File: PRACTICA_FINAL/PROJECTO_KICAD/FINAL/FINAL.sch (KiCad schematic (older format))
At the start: 0 parts

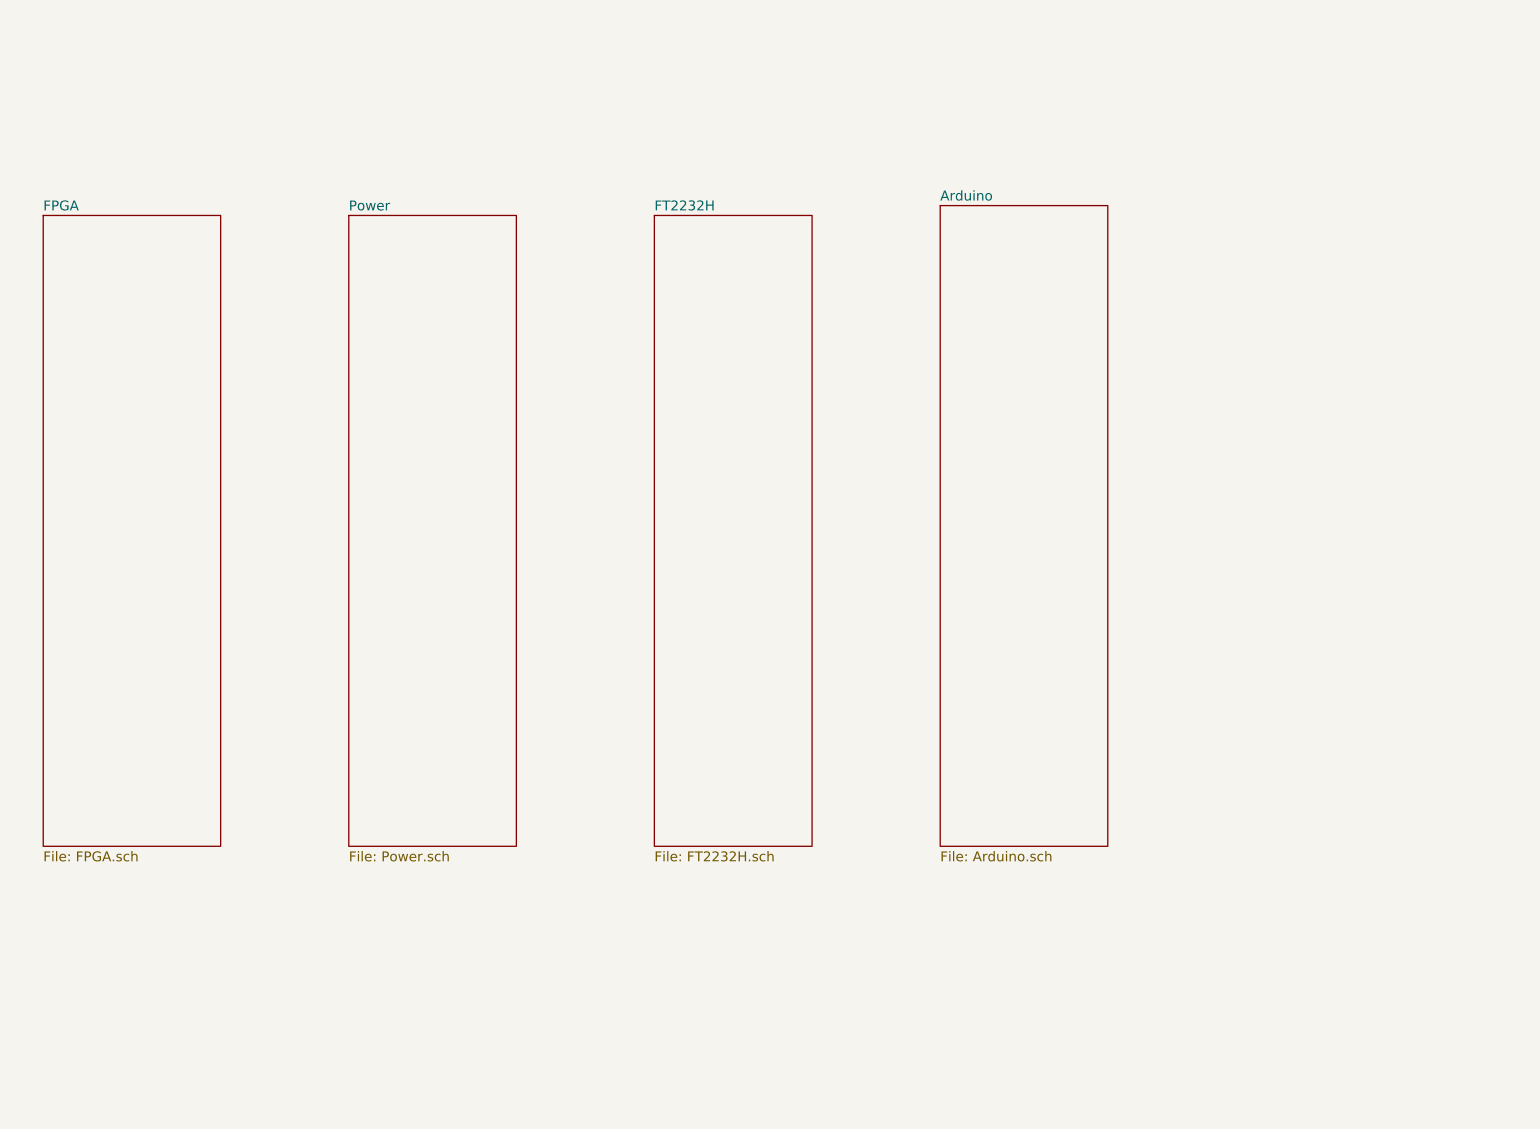
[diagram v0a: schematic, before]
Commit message: Terminada la hoja del FTDI y POWER y Arduino.bak FPGA terminado Power y Pheripheral. Lo principal de la cuestion del bnloque FPGA estan puestos los componentyes. Queda revisar globales y pasarlas a locales despues de eso. Un proyecto con muchas cosas globales se hace muy dificil de seguir.
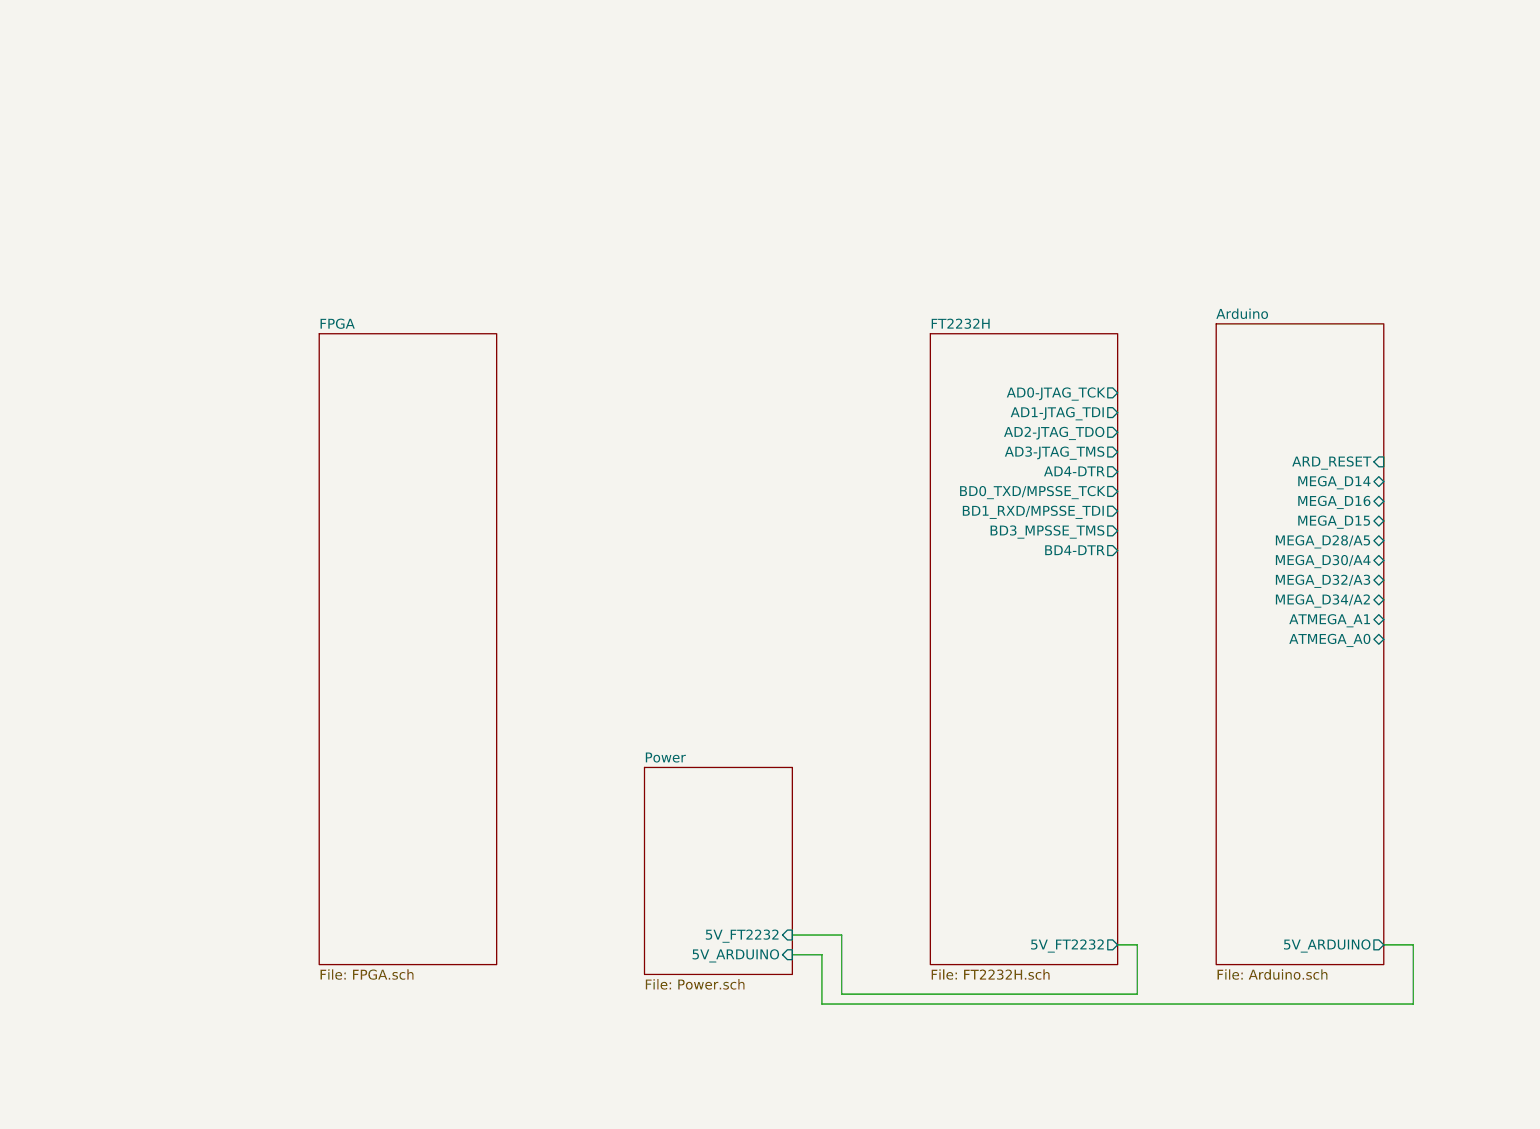
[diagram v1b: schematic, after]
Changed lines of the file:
@@
 EESchema Schematic File Version 4
+LIBS:FINAL-cache
 EELAYER 26 0
 EELAYER END
 $Descr A4 11693 8268
 encoding utf-8
-Sheet 1 5
+Sheet 1 8
 Title "Papillio Due - Clone"
 Date "2018-10-06"
@@
 $EndDescr
 $Sheet
-S 1800 1550 900  3200
+S 3200 2150 900  3200
 U 5BB93344
 F0 "FPGA" 50
@@
 $EndSheet
 $Sheet
-S 3350 1550 850  3200
+S 4850 4350 750  1050
 U 5BB93347
 F0 "Power" 50
 F1 "Power.sch" 50
+F2 "5V_ARDUINO" I R 5600 5300 50
+F3 "5V_FT2232" I R 5600 5200 50
 $EndSheet
 $Sheet
-S 4900 1550 800  3200
+S 6300 2150 950  3200
 U 5BB9334A
 F0 "FT2232H" 50
 F1 "FT2232H.sch" 50
+F2 "AD0-JTAG_TCK" O R 7250 2450 50
+F3 "AD1-JTAG_TDI" O R 7250 2550 50
+F4 "AD2-JTAG_TDO" O R 7250 2650 50
+F5 "AD3-JTAG_TMS" O R 7250 2750 50
+F6 "AD4-DTR" O R 7250 2850 50
+F7 "BD0_TXD/MPSSE_TCK" O R 7250 2950 50
+F8 "BD1_RXD/MPSSE_TDI" O R 7250 3050 50
+F9 "BD3_MPSSE_TMS" O R 7250 3150 50
+F10 "BD4-DTR" O R 7250 3250 50
+F11 "5V_FT2232" O R 7250 5250 50
 $EndSheet
 $Sheet
-S 6350 1500 850  3250
+S 7750 2100 850  3250
 U 5BB9334D
 F0 "Arduino" 50
 F1 "Arduino.sch" 50
+F2 "ARD_RESET" I R 8600 2800 50
+F3 "MEGA_D14" B R 8600 2900 50
+F4 "MEGA_D16" B R 8600 3000 50
+F5 "MEGA_D15" B R 8600 3100 50
+F6 "MEGA_D28/A5" B R 8600 3200 50
+F7 "MEGA_D30/A4" B R 8600 3300 50
+F8 "MEGA_D32/A3" B R 8600 3400 50
+F9 "MEGA_D34/A2" B R 8600 3500 50
+F10 "ATMEGA_A1" B R 8600 3600 50
+F11 "ATMEGA_A0" B R 8600 3700 50
+F12 "5V_ARDUINO" O R 8600 5250 50
 $EndSheet
+Wire Wire Line
+	5850 5500 7350 5500
+Wire Wire Line
+	7350 5500 7350 5250
+Wire Wire Line
+	7350 5250 7250 5250
+Wire Wire Line
+	5600 5300 5750 5300
+Wire Wire Line
+	5750 5300 5750 5550
+Wire Wire Line
+	5750 5550 8750 5550
+Wire Wire Line
+	8750 5550 8750 5250
+Wire Wire Line
+	8750 5250 8600 5250
+Wire Wire Line
+	5850 5200 5850 5500
+Wire Wire Line
+	5850 5200 5600 5200
 $EndSCHEMATC

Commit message: Actualizado el esquematico se enumera igual que el pdf. Se asignan todas las huellas lo unico que falta es la huella de un Arduino superpuesto Se corre DRC de esquematico y tambien se pasa a .NET y se levanta en el Kicad PCB sin errores
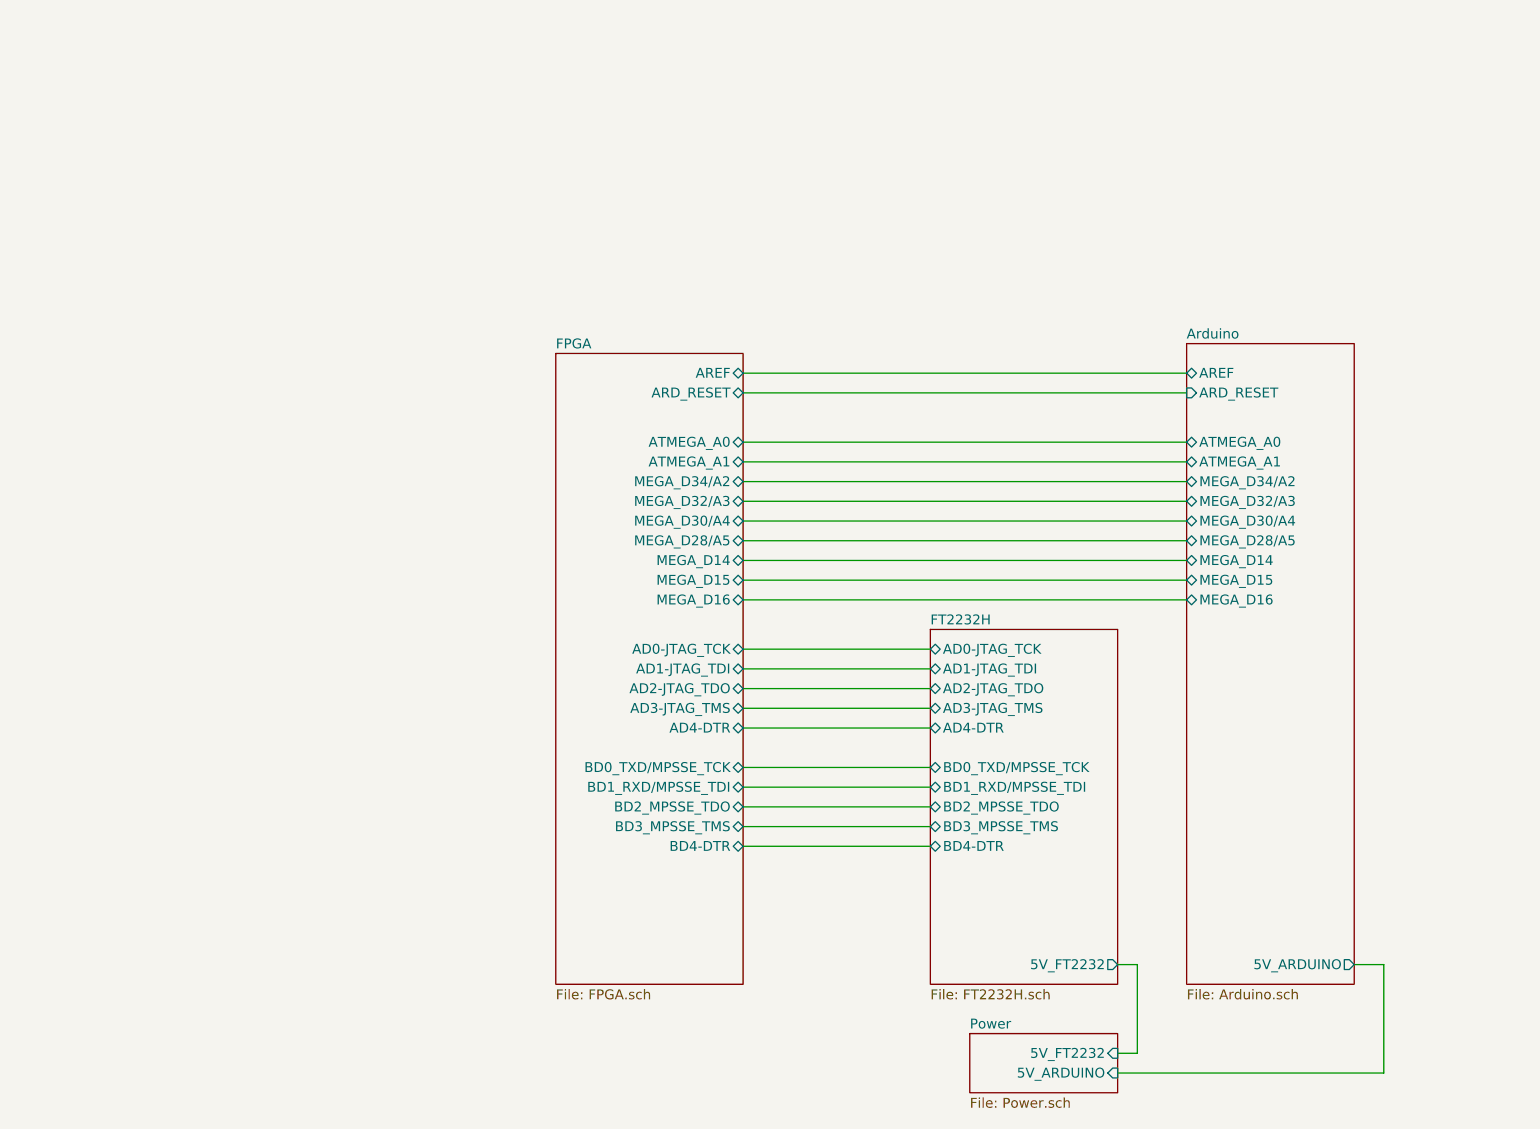
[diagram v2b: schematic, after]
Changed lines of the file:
@@
 $EndDescr
 $Sheet
-S 3200 2150 900  3200
+S 4400 2250 950  3200
 U 5BB93344
 F0 "FPGA" 50
 F1 "FPGA.sch" 50
+F2 "AD0-JTAG_TCK" B R 5350 3750 50
+F3 "AD2-JTAG_TDO" B R 5350 3950 50
+F4 "AD1-JTAG_TDI" B R 5350 3850 50
+F5 "AD3-JTAG_TMS" B R 5350 4050 50
+F6 "AD4-DTR" B R 5350 4150 50
+F7 "BD0_TXD/MPSSE_TCK" B R 5350 4350 50
+F8 "BD1_RXD/MPSSE_TDI" B R 5350 4450 50
+F9 "BD2_MPSSE_TDO" B R 5350 4550 50
+F10 "BD3_MPSSE_TMS" B R 5350 4650 50
+F11 "BD4-DTR" B R 5350 4750 50
+F12 "AREF" B R 5350 2350 50
+F13 "ARD_RESET" B R 5350 2450 50
+F14 "ATMEGA_A0" B R 5350 2700 50
+F15 "ATMEGA_A1" B R 5350 2800 50
+F16 "MEGA_D34/A2" B R 5350 2900 50
+F17 "MEGA_D32/A3" B R 5350 3000 50
+F18 "MEGA_D30/A4" B R 5350 3100 50
+F19 "MEGA_D28/A5" B R 5350 3200 50
+F20 "MEGA_D14" B R 5350 3300 50
+F21 "MEGA_D15" B R 5350 3400 50
+F22 "MEGA_D16" B R 5350 3500 50
 $EndSheet
 $Sheet
-S 4850 4350 750  1050
+S 6500 5700 750  300
 U 5BB93347
 F0 "Power" 50
 F1 "Power.sch" 50
-F2 "5V_ARDUINO" I R 5600 5300 50
-F3 "5V_FT2232" I R 5600 5200 50
+F2 "5V_ARDUINO" I R 7250 5900 50
+F3 "5V_FT2232" I R 7250 5800 50
 $EndSheet
 $Sheet
-S 6300 2150 950  3200
+S 7600 2200 850  3250
+U 5BB9334D
+F0 "Arduino" 50
+F1 "Arduino.sch" 50
+F2 "ARD_RESET" I L 7600 2450 50
+F3 "MEGA_D14" B L 7600 3300 50
+F4 "MEGA_D16" B L 7600 3500 50
+F5 "MEGA_D15" B L 7600 3400 50
+F6 "MEGA_D28/A5" B L 7600 3200 50
+F7 "MEGA_D30/A4" B L 7600 3100 50
+F8 "MEGA_D32/A3" B L 7600 3000 50
+F9 "MEGA_D34/A2" B L 7600 2900 50
+F10 "ATMEGA_A1" B L 7600 2800 50
+F11 "ATMEGA_A0" B L 7600 2700 50
+F12 "5V_ARDUINO" O R 8450 5350 50
+F13 "AREF" B L 7600 2350 50
+$EndSheet
+$Sheet
+S 6300 3650 950  1800
 U 5BB9334A
 F0 "FT2232H" 50
 F1 "FT2232H.sch" 50
-F2 "AD0-JTAG_TCK" O R 7250 2450 50
-F3 "AD1-JTAG_TDI" O R 7250 2550 50
-F4 "AD2-JTAG_TDO" O R 7250 2650 50
-F5 "AD3-JTAG_TMS" O R 7250 2750 50
-F6 "AD4-DTR" O R 7250 2850 50
-F7 "BD0_TXD/MPSSE_TCK" O R 7250 2950 50
-F8 "BD1_RXD/MPSSE_TDI" O R 7250 3050 50
-F9 "BD3_MPSSE_TMS" O R 7250 3150 50
-F10 "BD4-DTR" O R 7250 3250 50
-F11 "5V_FT2232" O R 7250 5250 50
-$EndSheet
-$Sheet
-S 7750 2100 850  3250
-U 5BB9334D
-F0 "Arduino" 50
-F1 "Arduino.sch" 50
-F2 "ARD_RESET" I R 8600 2800 50
-F3 "MEGA_D14" B R 8600 2900 50
-F4 "MEGA_D16" B R 8600 3000 50
-F5 "MEGA_D15" B R 8600 3100 50
-F6 "MEGA_D28/A5" B R 8600 3200 50
-F7 "MEGA_D30/A4" B R 8600 3300 50
-F8 "MEGA_D32/A3" B R 8600 3400 50
-F9 "MEGA_D34/A2" B R 8600 3500 50
-F10 "ATMEGA_A1" B R 8600 3600 50
-F11 "ATMEGA_A0" B R 8600 3700 50
-F12 "5V_ARDUINO" O R 8600 5250 50
+F2 "AD0-JTAG_TCK" B L 6300 3750 50
+F3 "AD1-JTAG_TDI" B L 6300 3850 50
+F4 "AD2-JTAG_TDO" B L 6300 3950 50
+F5 "AD3-JTAG_TMS" B L 6300 4050 50
+F6 "AD4-DTR" B L 6300 4150 50
+F7 "BD0_TXD/MPSSE_TCK" B L 6300 4350 50
+F8 "BD1_RXD/MPSSE_TDI" B L 6300 4450 50
+F9 "BD3_MPSSE_TMS" B L 6300 4650 50
+F10 "BD4-DTR" B L 6300 4750 50
+F11 "5V_FT2232" O R 7250 5350 50
+F12 "BD2_MPSSE_TDO" B L 6300 4550 50
 $EndSheet
 Wire Wire Line
-	5850 5500 7350 5500
+	5350 3500 7600 3500
 Wire Wire Line
-	7350 5500 7350 5250
+	5350 3400 7600 3400
 Wire Wire Line
-	7350 5250 7250 5250
+	7600 3300 5350 3300
 Wire Wire Line
-	5600 5300 5750 5300
+	5350 3200 7600 3200
 Wire Wire Line
-	5750 5300 5750 5550
+	5350 3100 7600 3100
 Wire Wire Line
-	5750 5550 8750 5550
+	5350 3000 7600 3000
 Wire Wire Line
-	8750 5550 8750 5250
+	5350 2900 7600 2900
 Wire Wire Line
-	8750 5250 8600 5250
+	5350 2800 7600 2800
 Wire Wire Line
-	5850 5200 5850 5500
+	5350 2700 7600 2700
 Wire Wire Line
-	5850 5200 5600 5200
+	5350 2350 7600 2350
+Wire Wire Line
+	5350 2450 7600 2450
+Wire Wire Line
+	6300 3750 5350 3750
+Wire Wire Line
+	5350 3850 6300 3850
+Wire Wire Line
+	5350 3950 6300 3950
+Wire Wire Line
+	5350 4050 6300 4050
+Wire Wire Line
+	5350 4150 6300 4150
+Wire Wire Line
+	5350 4350 6300 4350
+Wire Wire Line
+	5350 4450 6300 4450
+Wire Wire Line
+	5350 4550 6300 4550
+Wire Wire Line
+	6300 4650 5350 4650
+Wire Wire Line
+	5350 4750 6300 4750
+Wire Wire Line
+	7250 5350 7350 5350
+Wire Wire Line
+	7350 5350 7350 5800
+Wire Wire Line
+	7350 5800 7250 5800
+Wire Wire Line
+	7250 5900 8600 5900
+Wire Wire Line
+	8600 5900 8600 5350
+Wire Wire Line
+	8600 5350 8450 5350
 $EndSCHEMATC

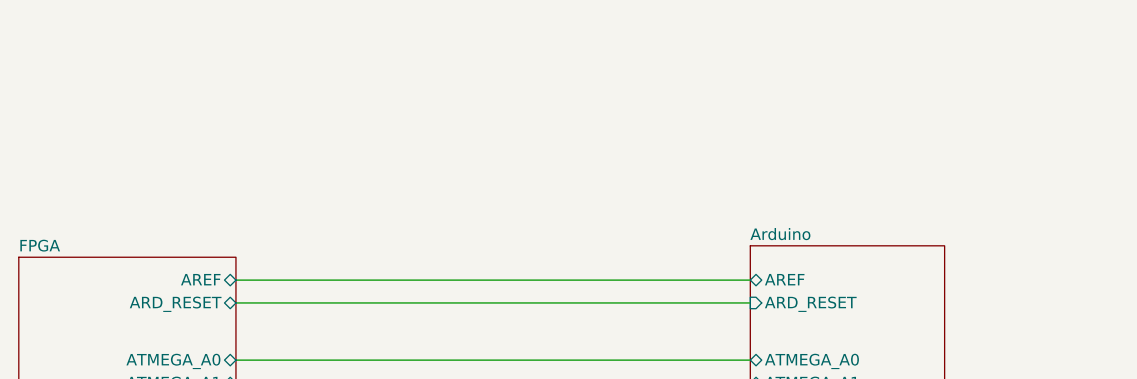
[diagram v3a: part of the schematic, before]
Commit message: Se agrega un mensaje en el top indicando donde se encuentra la informacion del HW el correspondiente link de la Papillio DUE.
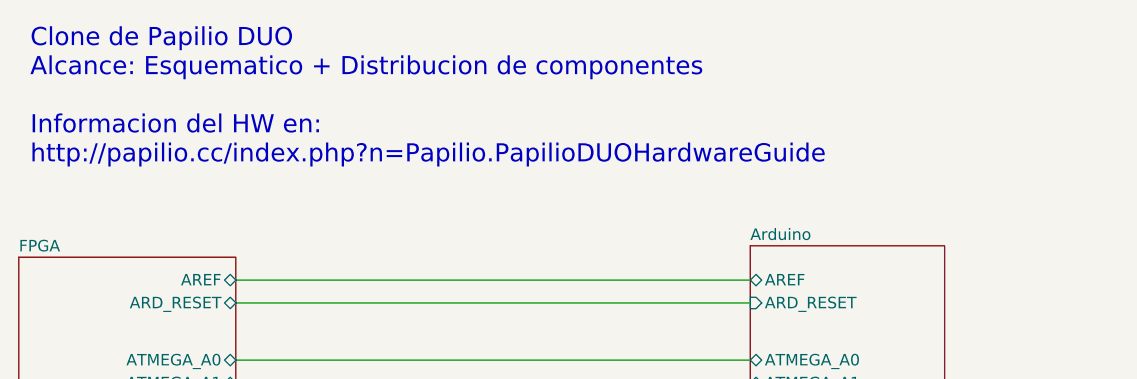
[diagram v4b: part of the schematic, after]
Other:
- note added: "Clone de Papilio DUO\nAlcance: Esquematico + Distribucion de componentes\n\nInformacion del HW en:\nhttp://papilio.cc/index.php?n=Papilio.PapilioDUOHardwareGuide"
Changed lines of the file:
@@
 Wire Wire Line
 	8600 5350 8450 5350
+Text Notes 4450 1850 0    79   ~ 0
+Clone de Papilio DUO\nAlcance: Esquematico + Distribucion de componentes\n\nInformacion del HW en:\nhttp://papilio.cc/index.php?n=Papilio.PapilioDUOHardwareGuide
 $EndSCHEMATC

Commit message: Se agrega Logos y Simbolos Se agrega fiduciales Se acomoda serigrafia para que sea visible y coherente Se agrega libreria de giduciales Se crea simbolo para el logo
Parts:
- added F1, F2, F3: Fiducial, Fiducial:Fiducial_1mm_Dia_2mm_Outer, symbol Mechanical:MountingHole
- added LOGO1: Logo_Open_Hardware_Small, Symbol:OSHW-Logo2_7.3x6mm_SilkScreen, symbol Graphic:Logo_Open_Hardware_Small
- added LOGO2: logo_glavigna, Symbol:KiCad-Logo2_6mm_SilkScreen, symbol Papilio_DUO-eagle-import:logo_glavigna
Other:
- note added: "Fiduciales"
- note added: "Symbols"
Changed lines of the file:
@@
 Wire Wire Line
 	8600 5350 8450 5350
-Text Notes 4450 1850 0    79   ~ 0
+Text Notes 4550 1750 0    79   ~ 0
 Clone de Papilio DUO\nAlcance: Esquematico + Distribucion de componentes\n\nInformacion del HW en:\nhttp://papilio.cc/index.php?n=Papilio.PapilioDUOHardwareGuide
+$Comp
+L Graphic:Logo_Open_Hardware_Small LOGO1
+U 1 1 5BD3CC36
+P 2500 1150
+F 0 "LOGO1" H 2500 1425 50  0001 C CNN
+F 1 "Logo_Open_Hardware_Small" H 2500 925 50  0001 C CNN
+F 2 "Symbol:OSHW-Logo2_7.3x6mm_SilkScreen" H 2500 1150 50  0001 C CNN
+F 3 "~" H 2500 1150 50  0001 C CNN
+	1    2500 1150
+	1    0    0    -1
+$EndComp
+$Comp
+L Mechanical:MountingHole F1
+U 1 1 5BD3CE11
+P 2250 2650
+F 0 "F1" H 2350 2696 50  0000 L CNN
+F 1 "Fiducial" H 2350 2605 50  0000 L CNN
+F 2 "Fiducial:Fiducial_1mm_Dia_2mm_Outer" H 2250 2650 50  0001 C CNN
+F 3 "~" H 2250 2650 50  0001 C CNN
+	1    2250 2650
+	1    0    0    -1
+$EndComp
+$Comp
+L Mechanical:MountingHole F2
+U 1 1 5BD3CE6F
+P 2250 3000
+F 0 "F2" H 2350 3046 50  0000 L CNN
+F 1 "Fiducial" H 2350 2955 50  0000 L CNN
+F 2 "Fiducial:Fiducial_1mm_Dia_2mm_Outer" H 2250 3000 50  0001 C CNN
+F 3 "~" H 2250 3000 50  0001 C CNN
+	1    2250 3000
+	1    0    0    -1
+$EndComp
+$Comp
+L Mechanical:MountingHole F3
+U 1 1 5BD3CE8D
+P 2250 3300
+F 0 "F3" H 2350 3346 50  0000 L CNN
+F 1 "Fiducial" H 2350 3255 50  0000 L CNN
+F 2 "Fiducial:Fiducial_1mm_Dia_2mm_Outer" H 2250 3300 50  0001 C CNN
+F 3 "~" H 2250 3300 50  0001 C CNN
+	1    2250 3300
+	1    0    0    -1
+$EndComp
+Text Notes 1950 2400 0    157  ~ 31
+Fiduciales
+Wire Notes Line
+	1800 2100 3250 2100
+Wire Notes Line
+	3250 2100 3250 3600
+Wire Notes Line
+	3250 3600 1800 3600
+Wire Notes Line
+	1800 3600 1800 2100
+Text Notes 2000 800  0    157  ~ 31
+Symbols
+Wire Notes Line
+	3250 550  3250 1900
+Wire Notes Line
+	3250 1900 1800 1900
+Wire Notes Line
+	1800 1900 1800 550
+Wire Notes Line
+	1800 550  3250 550
+$Comp
+L Papilio_DUO-eagle-import:logo_glavigna LOGO2
+U 1 1 5BD441DB
+P 2250 1550
+F 0 "LOGO2" H 2500 1600 50  0000 C CNN
+F 1 "logo_glavigna" H 2500 1350 50  0000 C CNN
+F 2 "Symbol:KiCad-Logo2_6mm_SilkScreen" H 2550 1500 50  0001 C CNN
+F 3 "" H 2550 1500 50  0001 C CNN
+	1    2250 1550
+	1    0    0    -1
+$EndComp
 $EndSCHEMATC
